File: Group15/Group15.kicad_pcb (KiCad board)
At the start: 4 copper layers, 100 x 100 mm, 3 parts, among them U1 RP2350A, U2 W25Q128JVS, Y1 ABM8-272-T3

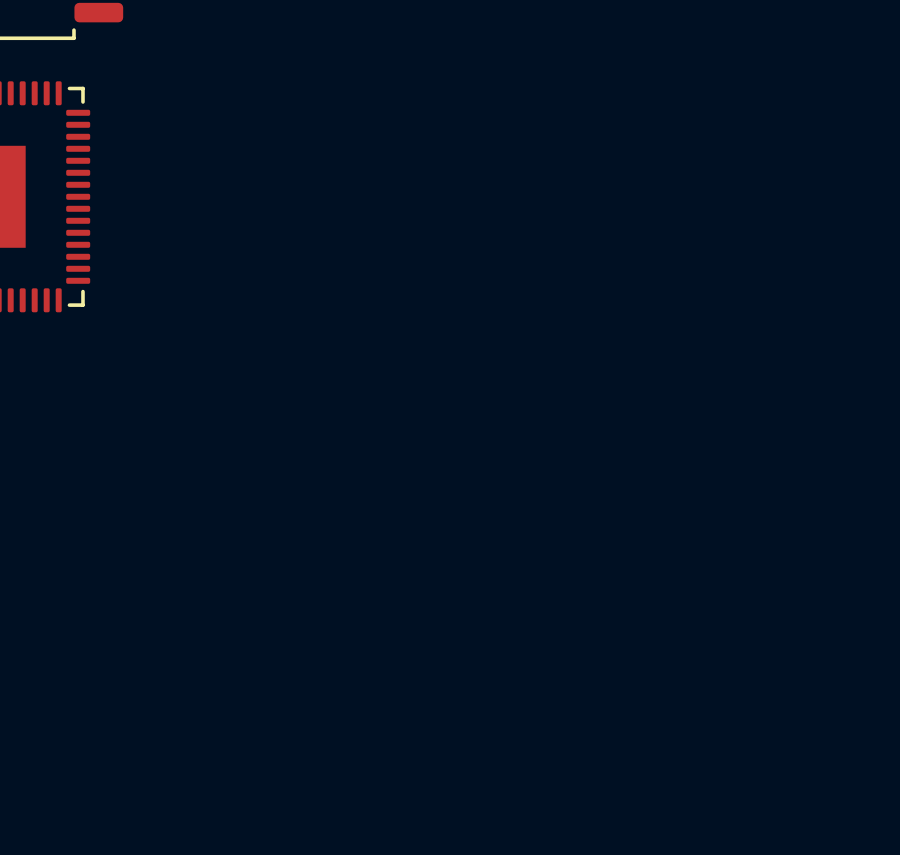
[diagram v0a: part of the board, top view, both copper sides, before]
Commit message: added Footprint for DAC
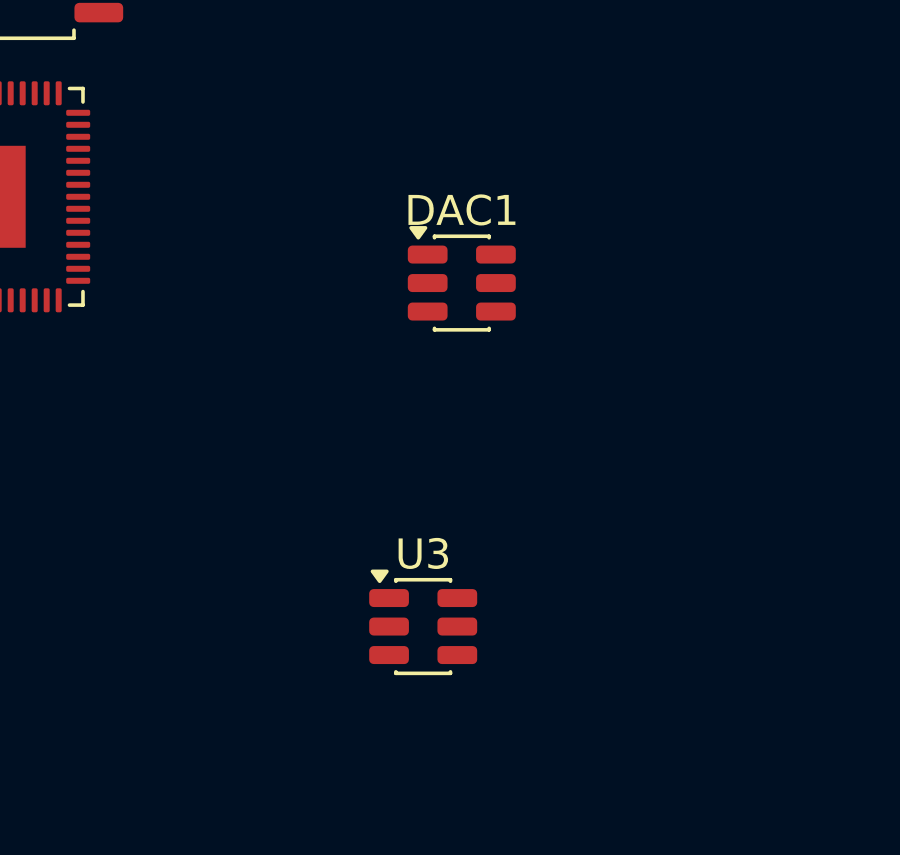
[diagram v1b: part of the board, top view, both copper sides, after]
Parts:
- added DAC1: ~, Package_TO_SOT_SMD:SOT-23-6, F.Cu at (153.9, 93.0)
- added U3: AP63205WU, Package_TO_SOT_SMD:TSOT-23-6, F.Cu at (152.6, 104.4)
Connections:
- U1 pad 2: unconnected-(U1-GPIO0-Pad2) -> +3V3
- U1 pad 51: unconnected-(U1-USB_DM-Pad51) -> Net-(U1-USB_DM)
- U1 pad 52: unconnected-(U1-USB_DP-Pad52) -> Net-(U1-USB_DP)
- U2 pad 1: unconnected-(U2-~{CS}-Pad1) -> +3V3
